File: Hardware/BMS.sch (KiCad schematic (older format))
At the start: 2 parts

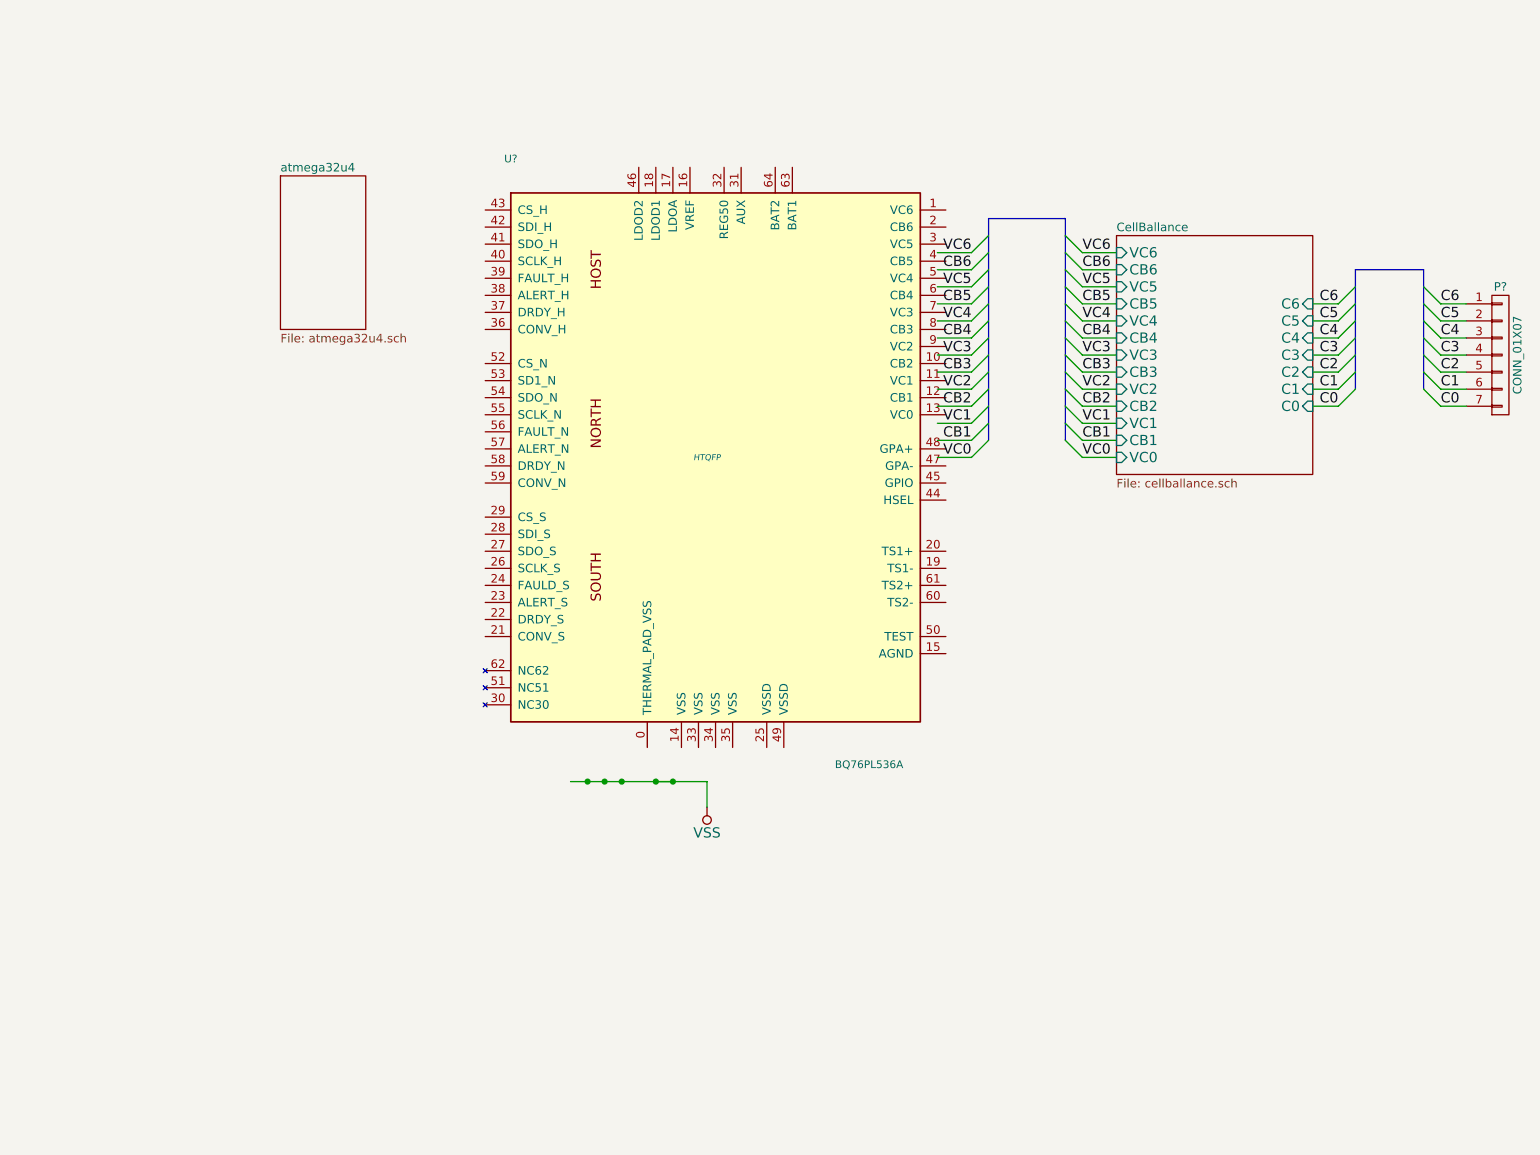
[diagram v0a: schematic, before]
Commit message: version 1 board completed
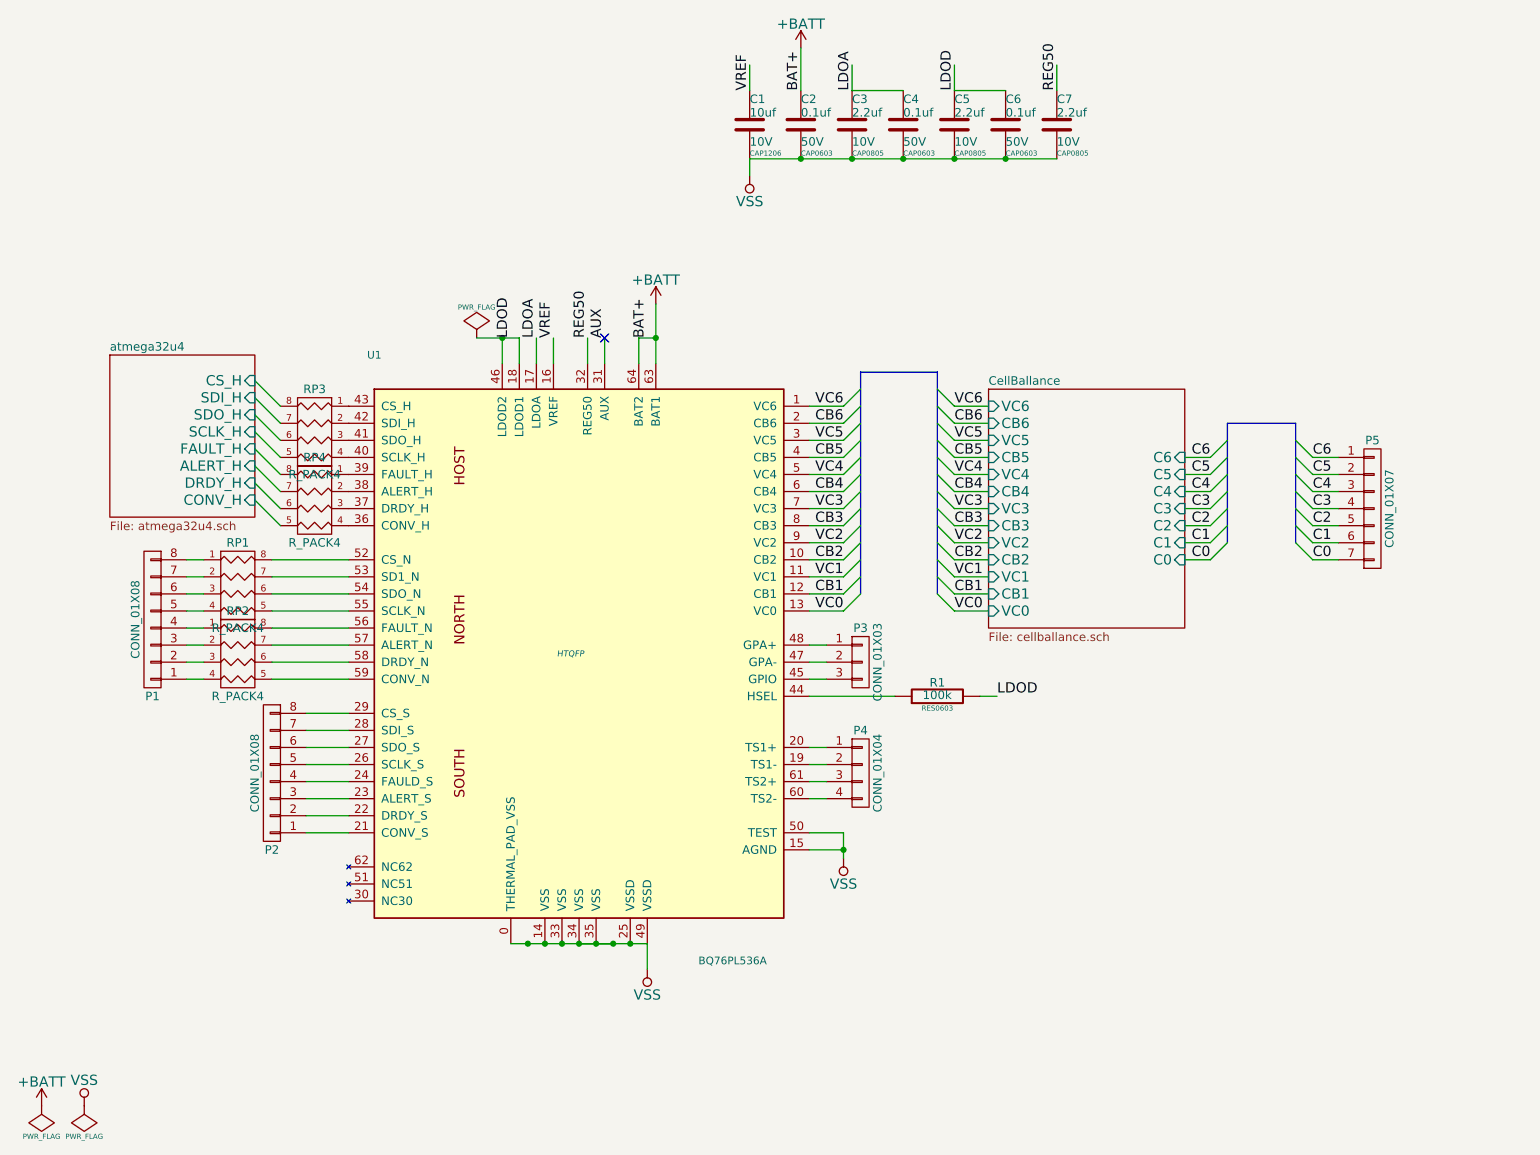
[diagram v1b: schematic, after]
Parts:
- added C1: 10uf, CAP1206, symbol C
- added C2, C4, C6: 0.1uf, CAP0603, symbol C
- added C3, C5, C7: 2.2uf, CAP0805, symbol C
- added P1, P2: CONN_01X08, symbol CONN_01X08
- added P3: CONN_01X03, symbol CONN_01X03
- added P4: CONN_01X04, symbol CONN_01X04
- added R1: 100k, RES0603, symbol R
- added RP1, RP2, RP3, RP4: R_PACK4, symbol R_PACK4
- gave numbers to parts that had none: 2
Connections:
- net labels added: +BATT, AUX, BAT+, LDOA, LDOD, REG50, VREF
- wire segments 43 -> 106
- no-connect marks 0 -> 1
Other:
- moved on the sheet: P5, U1
